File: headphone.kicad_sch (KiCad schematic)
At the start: 2 parts

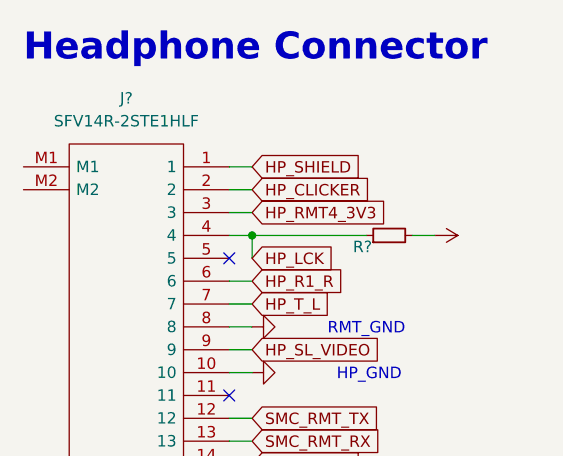
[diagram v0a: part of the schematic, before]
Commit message: schem: first pass done, ERC passing
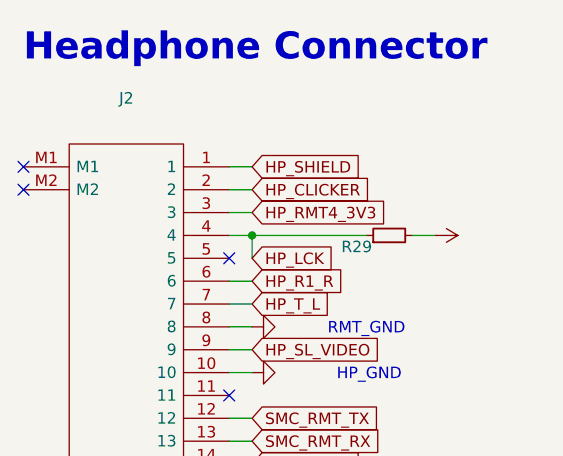
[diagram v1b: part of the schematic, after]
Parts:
- J2: renamed from J?; value SFV14R-2STE1HLF -> (none)
- gave numbers to parts that had none: 1
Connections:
- no-connect marks 2 -> 4
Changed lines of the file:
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@@
   )
   (no_connect (at 130.81 111.76))
+  (no_connect (at 107.95 101.6))
+  (no_connect (at 107.95 104.14))
   (no_connect (at 130.81 127))
   (wire (pts (xy 130.81 116.84) (xy 133.35 116.84))
@@
   (symbol (lib_id "power:GNDA") (at 133.35 124.46 90) (unit 1)
     (in_bom yes) (on_board yes) (fields_autoplaced)
-    (property "Reference" "#PWR?" (id 0) (at 139.7 124.46 0)
+    (property "Reference" "#PWR067" (id 0) (at 139.7 124.46 0)
       (effects (font (size 1.27 1.27)) hide)
     )
@@
   (symbol (lib_id "power:+3.3V") (at 153.67 109.22 270) (unit 1)
     (in_bom yes) (on_board yes) (fields_autoplaced)
-    (property "Reference" "#PWR?" (id 0) (at 149.86 109.22 0)
+    (property "Reference" "#PWR068" (id 0) (at 149.86 109.22 0)
       (effects (font (size 1.27 1.27)) hide)
     )
@@
   (symbol (lib_id "power:GND") (at 133.35 119.38 90) (unit 1)
     (in_bom yes) (on_board yes) (fields_autoplaced)
-    (property "Reference" "#PWR?" (id 0) (at 139.7 119.38 0)
+    (property "Reference" "#PWR066" (id 0) (at 139.7 119.38 0)
       (effects (font (size 1.27 1.27)) hide)
     )
@@
   (symbol (lib_id "gigahawk:SFV14R-2STE1HLF") (at 107.95 101.6 0) (unit 1)
     (in_bom yes) (on_board yes) (fields_autoplaced)
-    (property "Reference" "J?" (id 0) (at 119.38 93.98 0))
-    (property "Value" "SFV14R-2STE1HLF" (id 1) (at 119.38 96.52 0))
+    (property "Reference" "J2" (id 0) (at 119.38 93.98 0))
+    (property "Value" "" (id 1) (at 119.38 96.52 0))
     (property "Footprint" "Gigahawk:SFV14R2STE1HLF" (id 2) (at 127 99.06 0)
       (effects (font (size 1.27 1.27)) (justify left) hide)
@@
   (symbol (lib_id "Device:R_Small") (at 148.59 109.22 90) (unit 1)
     (in_bom yes) (on_board yes)
-    (property "Reference" "R?" (id 0) (at 146.685 110.49 90)
+    (property "Reference" "R29" (id 0) (at 146.685 110.49 90)
       (effects (font (size 1.27 1.27)) (justify left))
     )

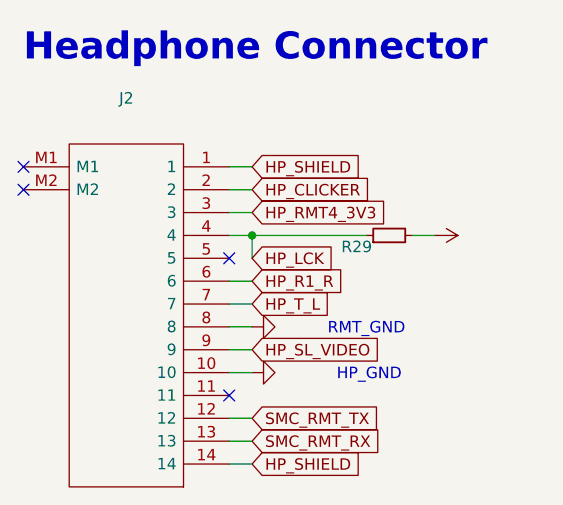
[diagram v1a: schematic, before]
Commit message: analysis: specify pi will be powered directly from VCC
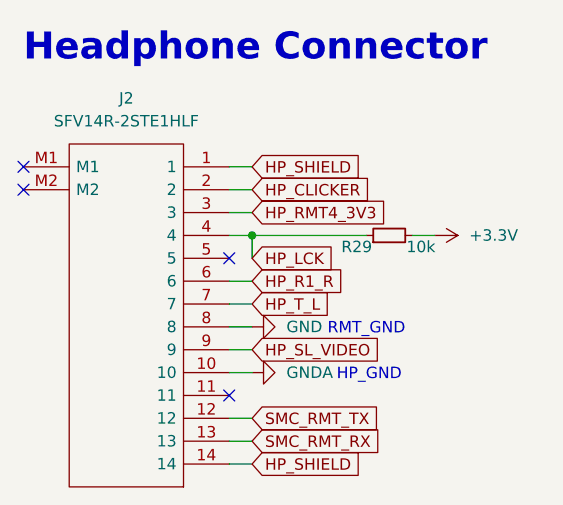
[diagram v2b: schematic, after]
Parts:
- J2: value (none) -> SFV14R-2STE1HLF
- R29: value (none) -> 10k; footprint (none) -> Resistor_SMD:R_0402_1005Metric
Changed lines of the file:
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@@
       (effects (font (size 1.27 1.27)) hide)
     )
-    (property "Value" "" (id 1) (at 137.16 124.4599 90)
+    (property "Value" "GNDA" (id 1) (at 137.16 124.4599 90)
       (effects (font (size 1.27 1.27)) (justify right))
     )
@@
       (effects (font (size 1.27 1.27)) hide)
     )
-    (property "Value" "" (id 1) (at 157.48 109.2199 90)
+    (property "Value" "+3.3V" (id 1) (at 157.48 109.2199 90)
       (effects (font (size 1.27 1.27)) (justify left))
     )
@@
       (effects (font (size 1.27 1.27)) hide)
     )
-    (property "Value" "" (id 1) (at 137.16 119.3799 90)
+    (property "Value" "GND" (id 1) (at 137.16 119.3799 90)
       (effects (font (size 1.27 1.27)) (justify right))
     )
@@
     (in_bom yes) (on_board yes) (fields_autoplaced)
     (property "Reference" "J2" (id 0) (at 119.38 93.98 0))
-    (property "Value" "" (id 1) (at 119.38 96.52 0))
+    (property "Value" "SFV14R-2STE1HLF" (id 1) (at 119.38 96.52 0))
     (property "Footprint" "Gigahawk:SFV14R2STE1HLF" (id 2) (at 127 99.06 0)
       (effects (font (size 1.27 1.27)) (justify left) hide)
@@
       (effects (font (size 1.27 1.27)) (justify left))
     )
-    (property "Value" "" (id 1) (at 150.495 110.49 90)
+    (property "Value" "10k" (id 1) (at 150.495 110.49 90)
       (effects (font (size 1.27 1.27)) (justify right))
     )
-    (property "Footprint" "" (id 2) (at 148.59 109.22 0)
+    (property "Footprint" "Resistor_SMD:R_0402_1005Metric" (id 2) (at 148.59 109.22 0)
       (effects (font (size 1.27 1.27)) hide)
     )

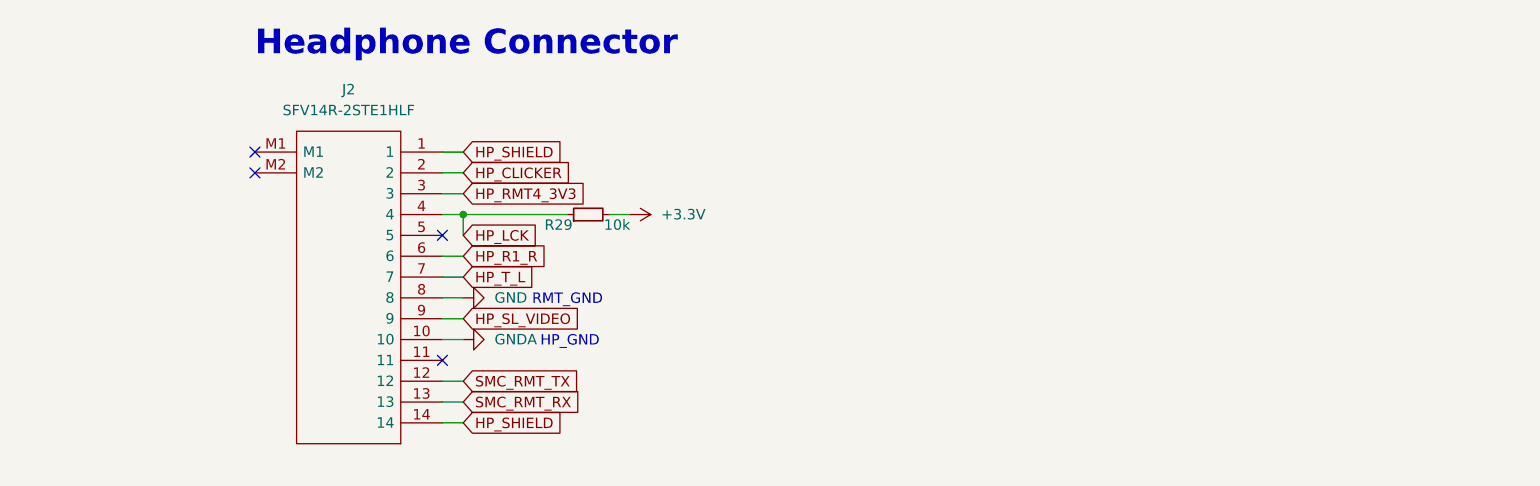
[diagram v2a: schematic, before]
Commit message: schem: add MOSFET to drive clickwheel
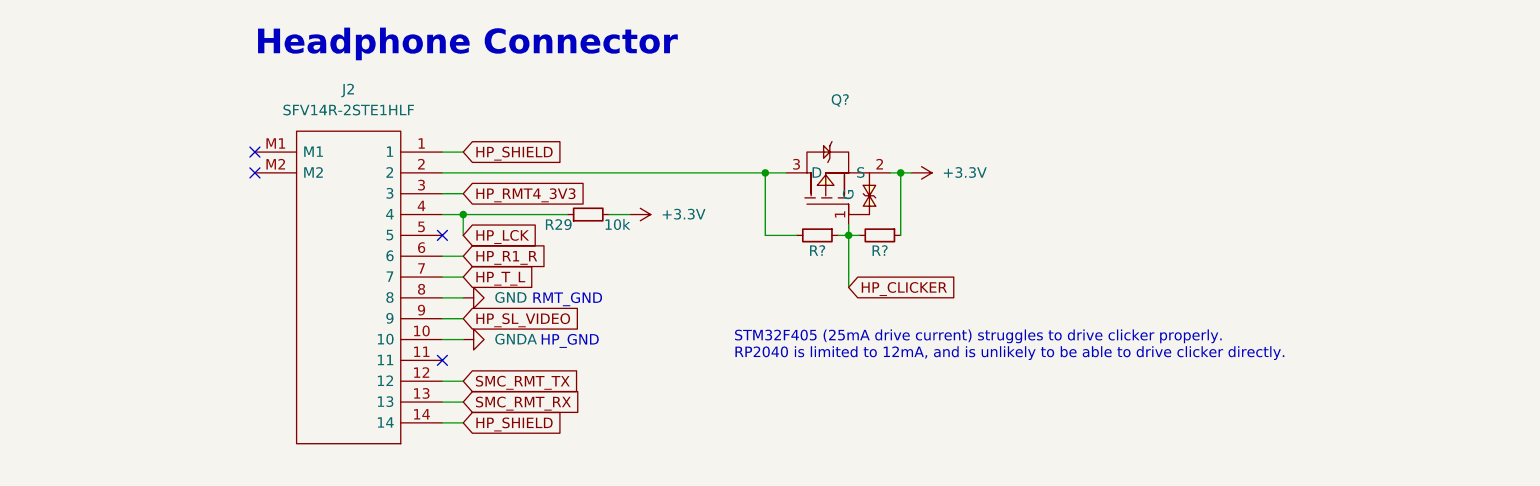
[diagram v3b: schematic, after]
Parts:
- added Q?: (no value), lcsc:SOT-723_L1.2-W0.8-P0.40-LS1.2-BR, symbol lcsc:TPNTK3139PT1G
- added R? (x2): (no value), symbol Device:R_Small
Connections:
- net +3V3: now also Q?.2 (S), R?.1
- net HP_CLICKER: now also Q?.1 (G), R?.1, R?.2; no longer J2.2
- new net: J2.2, Q?.3 (D), R?.2
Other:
- note added: "STM32F405 (25mA drive current) struggles to drive clicker properly. RP2040 is limited to 12mA, and is unlikely to be able to drive clicker directly."
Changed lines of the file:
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@@
 (kicad_sch (version 20211123) (generator eeschema)
   (paper "A4")
+  (junction (at 180.34 111.76) (diameter 0) (color 0 0 0 0)
+  )
+  (junction (at 170.18 104.14) (diameter 0) (color 0 0 0 0)
+  )
+  (junction (at 186.69 104.14) (diameter 0) (color 0 0 0 0)
+  )
   (junction (at 133.35 109.22) (diameter 0) (color 0 0 0 0)
   )
@@
   (no_connect (at 107.95 104.14))
   (no_connect (at 130.81 127))
+  (wire (pts (xy 180.34 111.76) (xy 180.34 110.49))
+    (stroke (width 0) (type default) (color 0 0 0 0))
+  )
   (wire (pts (xy 130.81 116.84) (xy 133.35 116.84))
     (stroke (width 0) (type default) (color 0 0 0 0))
   )
+  (wire (pts (xy 186.69 104.14) (xy 186.69 111.76))
+    (stroke (width 0) (type default) (color 0 0 0 0))
+  )
   (wire (pts (xy 130.81 129.54) (xy 133.35 129.54))
     (stroke (width 0) (type default) (color 0 0 0 0))
   )
+  (wire (pts (xy 180.34 111.76) (xy 180.34 118.11))
+    (stroke (width 0) (type default) (color 0 0 0 0))
+  )
   (wire (pts (xy 130.81 109.22) (xy 133.35 109.22))
     (stroke (width 0) (type default) (color 0 0 0 0))
   )
-  (wire (pts (xy 130.81 104.14) (xy 133.35 104.14))
+  (wire (pts (xy 130.81 104.14) (xy 170.18 104.14))
     (stroke (width 0) (type default) (color 0 0 0 0))
   )
@@
     (stroke (width 0) (type default) (color 0 0 0 0))
   )
+  (wire (pts (xy 186.69 104.14) (xy 187.96 104.14))
+    (stroke (width 0) (type default) (color 0 0 0 0))
+  )
+  (wire (pts (xy 185.42 104.14) (xy 186.69 104.14))
+    (stroke (width 0) (type default) (color 0 0 0 0))
+  )
+  (wire (pts (xy 173.99 111.76) (xy 170.18 111.76))
+    (stroke (width 0) (type default) (color 0 0 0 0))
+  )
   (wire (pts (xy 133.35 109.22) (xy 133.35 111.76))
     (stroke (width 0) (type default) (color 0 0 0 0))
@@
     (stroke (width 0) (type default) (color 0 0 0 0))
   )
+  (wire (pts (xy 181.61 111.76) (xy 180.34 111.76))
+    (stroke (width 0) (type default) (color 0 0 0 0))
+  )
   (wire (pts (xy 130.81 121.92) (xy 133.35 121.92))
     (stroke (width 0) (type default) (color 0 0 0 0))
@@
     (stroke (width 0) (type default) (color 0 0 0 0))
   )
+  (wire (pts (xy 179.07 111.76) (xy 180.34 111.76))
+    (stroke (width 0) (type default) (color 0 0 0 0))
+  )
   (wire (pts (xy 130.81 114.3) (xy 133.35 114.3))
     (stroke (width 0) (type default) (color 0 0 0 0))
   )
   (wire (pts (xy 130.81 101.6) (xy 133.35 101.6))
+    (stroke (width 0) (type default) (color 0 0 0 0))
+  )
+  (wire (pts (xy 170.18 111.76) (xy 170.18 104.14))
+    (stroke (width 0) (type default) (color 0 0 0 0))
+  )
+  (wire (pts (xy 170.18 104.14) (xy 172.72 104.14))
     (stroke (width 0) (type default) (color 0 0 0 0))
   )
@@
     (effects (font (size 3 3) (thickness 0.6) bold) (justify left bottom))
   )
+  (text "STM32F405 (25mA drive current) struggles to drive clicker properly.\nRP2040 is limited to 12mA, and is unlikely to be able to drive clicker directly."
+    (at 166.37 127 0)
+    (effects (font (size 1.27 1.27)) (justify left bottom))
+  )
   (text "HP_GND" (at 142.748 125.476 0)
     (effects (font (size 1.27 1.27)) (justify left bottom))
@@
     )
   )
-  (global_label "HP_CLICKER" (shape input) (at 133.35 104.14 0) (fields_autoplaced)
-    (effects (font (size 1.27 1.27)) (justify left))
-    (property "Intersheet References" "${INTERSHEET_REFS}" (id 0) (at 147.1931 104.0606 0)
+  (global_label "HP_CLICKER" (shape input) (at 180.34 118.11 0) (fields_autoplaced)
+    (effects (font (size 1.27 1.27)) (justify left))
+    (property "Intersheet References" "${INTERSHEET_REFS}" (id 0) (at 194.1831 118.0306 0)
       (effects (font (size 1.27 1.27)) (justify left) hide)
     )
@@
       (effects (font (size 1.27 1.27)) (justify left) hide)
     )
+  )
+  (symbol (lib_id "lcsc:TPNTK3139PT1G") (at 177.8 104.14 90) (unit 1)
+    (in_bom yes) (on_board yes) (fields_autoplaced)
+    (property "Reference" "Q?" (id 0) (at 179.325 95.25 90))
+    (property "Value" "" (id 1) (at 179.325 97.79 90))
+    (property "Footprint" "lcsc:SOT-723_L1.2-W0.8-P0.40-LS1.2-BR" (id 2) (at 190.5 104.14 0)
+      (effects (font (size 1.27 1.27)) hide)
+    )
+    (property "Datasheet" "https://lcsc.com/product-detail/MOSFET_TECH-PUBLIC-TPNTK3139PT1G_C558623.html" (id 3) (at 193.04 104.14 0)
+      (effects (font (size 1.27 1.27)) hide)
+    )
+    (property "Manufacturer" "TECH PUBLIC" (id 4) (at 195.58 104.14 0)
+      (effects (font (size 1.27 1.27)) hide)
+    )
+    (property "LCSC Part" "C558623" (id 5) (at 198.12 104.14 0)
+      (effects (font (size 1.27 1.27)) hide)
+    )
+    (property "JLC Part" "Extended Part" (id 6) (at 200.66 104.14 0)
+      (effects (font (size 1.27 1.27)) hide)
+    )
+    (pin "1")
+    (pin "2")
+    (pin "3")
   )
   (symbol (lib_id "power:GNDA") (at 133.35 124.46 90) (unit 1)
@@
     (pin "1")
   )
+  (symbol (lib_id "Device:R_Small") (at 184.15 111.76 270) (unit 1)
+    (in_bom yes) (on_board yes)
+    (property "Reference" "R?" (id 0) (at 184.15 113.665 90))
+    (property "Value" "" (id 1) (at 184.15 115.57 90))
+    (property "Footprint" "" (id 2) (at 184.15 111.76 0)
+      (effects (font (size 1.27 1.27)) hide)
+    )
+    (property "Datasheet" "~" (id 3) (at 184.15 111.76 0)
+      (effects (font (size 1.27 1.27)) hide)
+    )
+    (pin "1")
+    (pin "2")
+  )
   (symbol (lib_id "power:+3.3V") (at 153.67 109.22 270) (unit 1)
     (in_bom yes) (on_board yes) (fields_autoplaced)
@@
     )
     (property "Datasheet" "" (id 3) (at 133.35 119.38 0)
+      (effects (font (size 1.27 1.27)) hide)
+    )
+    (pin "1")
+  )
+  (symbol (lib_id "power:+3.3V") (at 187.96 104.14 270) (unit 1)
+    (in_bom yes) (on_board yes) (fields_autoplaced)
+    (property "Reference" "#PWR?" (id 0) (at 184.15 104.14 0)
+      (effects (font (size 1.27 1.27)) hide)
+    )
+    (property "Value" "+3.3V" (id 1) (at 191.77 104.1399 90)
+      (effects (font (size 1.27 1.27)) (justify left))
+    )
+    (property "Footprint" "" (id 2) (at 187.96 104.14 0)
+      (effects (font (size 1.27 1.27)) hide)
+    )
+    (property "Datasheet" "" (id 3) (at 187.96 104.14 0)
       (effects (font (size 1.27 1.27)) hide)
     )
@@
     (pin "M2")
   )
+  (symbol (lib_id "Device:R_Small") (at 176.53 111.76 270) (unit 1)
+    (in_bom yes) (on_board yes)
+    (property "Reference" "R?" (id 0) (at 176.53 113.665 90))
+    (property "Value" "" (id 1) (at 176.53 115.57 90))
+    (property "Footprint" "" (id 2) (at 176.53 111.76 0)
+      (effects (font (size 1.27 1.27)) hide)
+    )
+    (property "Datasheet" "~" (id 3) (at 176.53 111.76 0)
+      (effects (font (size 1.27 1.27)) hide)
+    )
+    (pin "1")
+    (pin "2")
+  )
   (symbol (lib_id "Device:R_Small") (at 148.59 109.22 90) (unit 1)

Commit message: layout: switch to lcsc fpc connectors
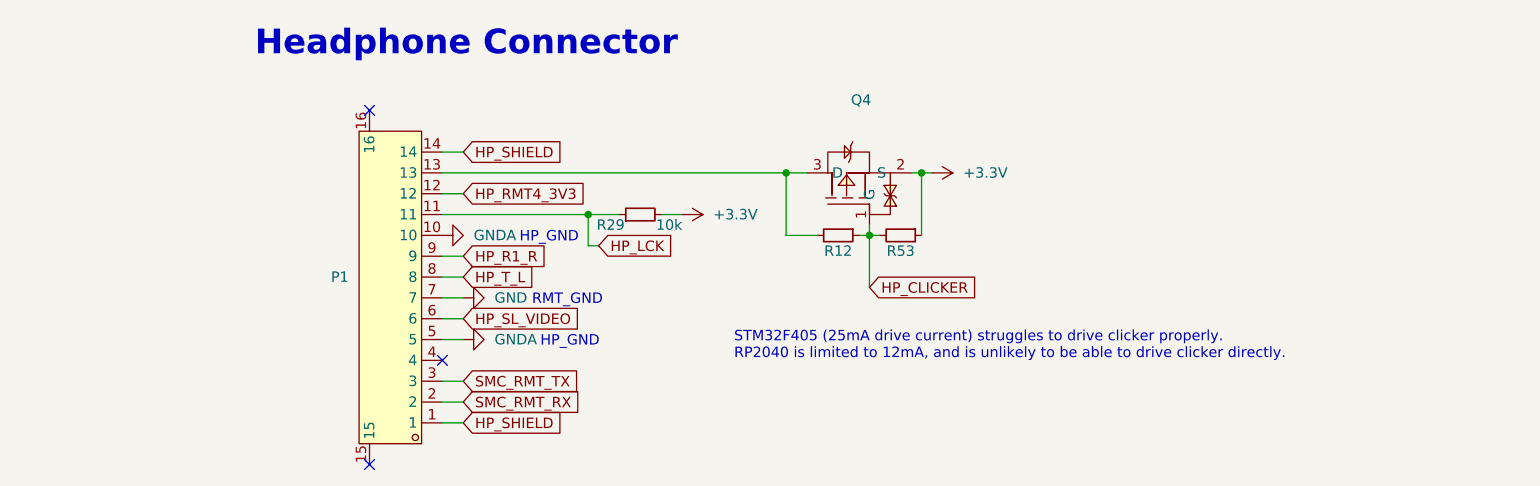
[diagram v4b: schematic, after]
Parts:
- removed J2: SFV14R-2STE1HLF, Gigahawk:SFV14R2STE1HLF, symbol gigahawk:SFV14R-2STE1HLF
- added P1: (no value), symbol lcsc:FPC0.5MM14PPulltypeH2.0mmPickup
- gave numbers to parts that had none: 3
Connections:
- net GND: now also P1.7
- net GNDA: now also P1.10, P1.5
- net HP_LCK: now also P1.11
- net HP_R1_R: now also P1.9
- net HP_RMT4_3V3: now also P1.12
- net HP_SHIELD: now also P1.1, P1.14
- net HP_SL_VIDEO: now also P1.6
- net HP_T_L: now also P1.8
- net SMC_RMT_RX: now also P1.2
- net SMC_RMT_TX: now also P1.3
- net at Q4.3 (D), R12.2: now also P1.13
- no-connect marks 4 -> 3
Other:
- moved on the sheet: Q4, R12, R29, R53

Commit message: integration: add mounting holes and connectors and second board
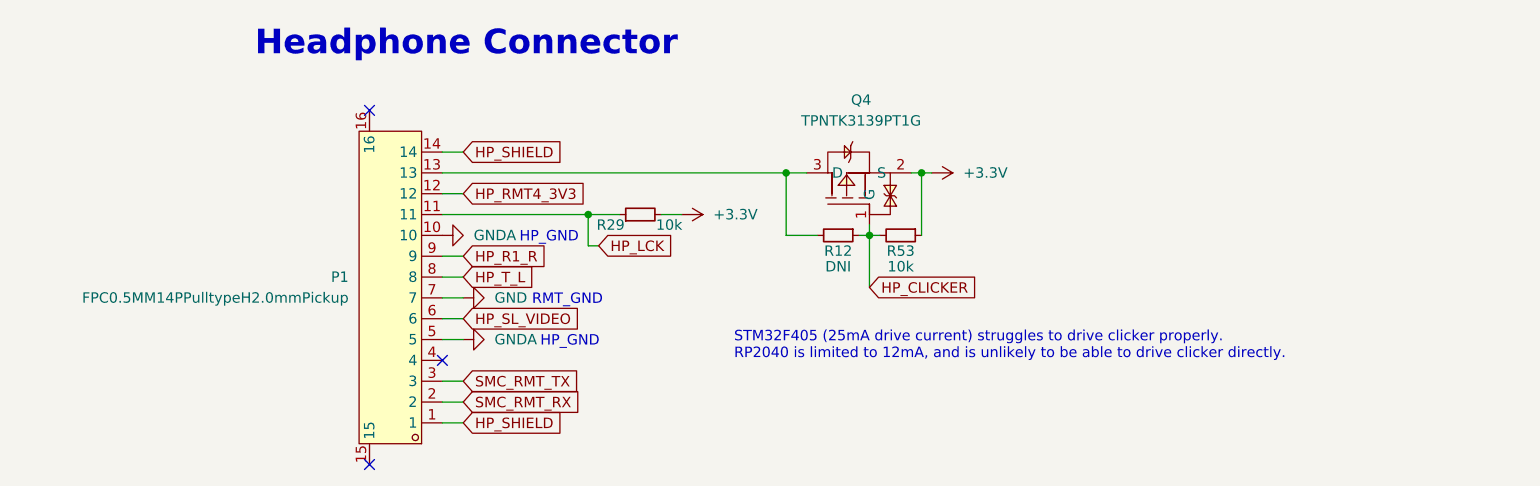
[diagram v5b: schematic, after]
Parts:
- P1: value (none) -> FPC0.5MM14PPulltypeH2.0mmPickup; footprint (none) -> lcsc:FPC-SMD_14P-L12.5-W5.4-P0.50
- Q4: value (none) -> TPNTK3139PT1G
- R12: value (none) -> DNI; footprint (none) -> Resistor_SMD:R_0402_1005Metric
- R53: value (none) -> 10k; footprint (none) -> Resistor_SMD:R_0402_1005Metric
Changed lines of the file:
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@@
     (in_bom yes) (on_board yes) (fields_autoplaced)
     (property "Reference" "Q4" (id 0) (at 181.865 95.25 90))
-    (property "Value" "" (id 1) (at 181.865 97.79 90))
+    (property "Value" "TPNTK3139PT1G" (id 1) (at 181.865 97.79 90))
     (property "Footprint" "lcsc:SOT-723_L1.2-W0.8-P0.40-LS1.2-BR" (id 2) (at 193.04 104.14 0)
       (effects (font (size 1.27 1.27)) hide)
@@
       (effects (font (size 1.27 1.27)) (justify left))
     )
-    (property "Value" "" (id 1) (at 119.38 119.3799 0)
+    (property "Value" "FPC0.5MM14PPulltypeH2.0mmPickup" (id 1) (at 119.38 119.3799 0)
       (effects (font (size 1.27 1.27)) (justify left))
     )
-    (property "Footprint" "" (id 2) (at 127 88.9 0)
+    (property "Footprint" "lcsc:FPC-SMD_14P-L12.5-W5.4-P0.50" (id 2) (at 127 88.9 0)
       (effects (font (size 1.27 1.27)) hide)
     )
@@
     (in_bom yes) (on_board yes)
     (property "Reference" "R53" (id 0) (at 186.69 113.665 90))
-    (property "Value" "" (id 1) (at 186.69 115.57 90))
-    (property "Footprint" "" (id 2) (at 186.69 111.76 0)
+    (property "Value" "10k" (id 1) (at 186.69 115.57 90))
+    (property "Footprint" "Resistor_SMD:R_0402_1005Metric" (id 2) (at 186.69 111.76 0)
       (effects (font (size 1.27 1.27)) hide)
     )
@@
     (in_bom yes) (on_board yes)
     (property "Reference" "R12" (id 0) (at 179.07 113.665 90))
-    (property "Value" "" (id 1) (at 179.07 115.57 90))
-    (property "Footprint" "" (id 2) (at 179.07 111.76 0)
+    (property "Value" "DNI" (id 1) (at 179.07 115.57 90))
+    (property "Footprint" "Resistor_SMD:R_0402_1005Metric" (id 2) (at 179.07 111.76 0)
       (effects (font (size 1.27 1.27)) hide)
     )
